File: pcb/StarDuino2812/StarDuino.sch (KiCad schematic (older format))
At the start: 86 parts, among them J1 Screw_Terminal_01x02, J2 Conn_01x03_Male, J3 Conn_01x01_Male, Q1 IRLML6401, U1 ATmega328P-AU, Y1 16M

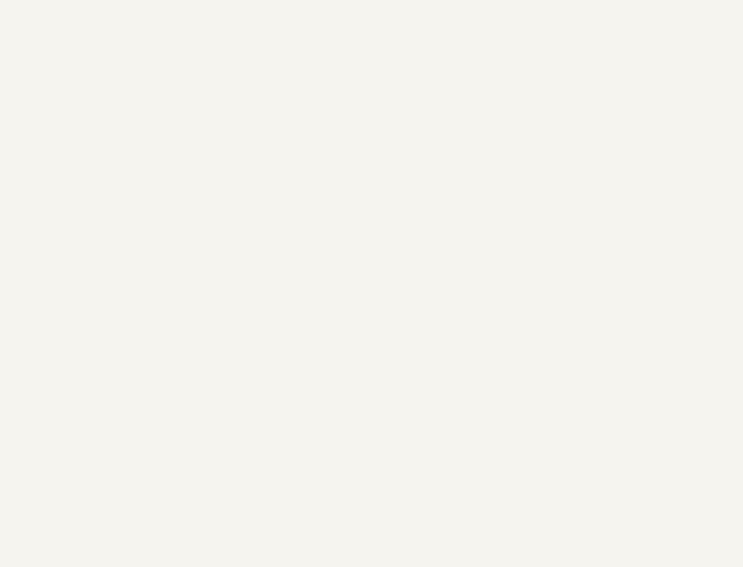
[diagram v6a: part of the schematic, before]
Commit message: NewYearStar2812. Add capacitors.
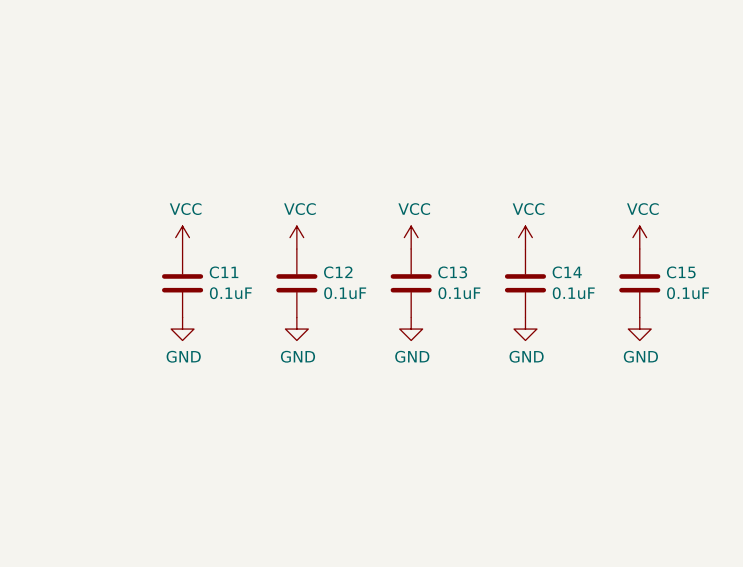
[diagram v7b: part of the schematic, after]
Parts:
- added C11, C12, C13, C14, C15: 0.1uF, Capacitor_THT:C_Rect_L19.0mm_W5.0mm_P15.00mm_MKS4, symbol Device:C
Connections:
- net GND: now also C11.2, C12.2, C13.2, C14.2, C15.2
- net VCC: now also C11.1, C12.1, C13.1, C14.1, C15.1
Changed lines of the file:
@@
 Wire Wire Line
 	4050 6050 4150 6050
+$Comp
+L Device:C C11
+U 1 1 61480CBF
+P 11500 13900
+F 0 "C11" H 11615 13946 50  0000 L CNN
+F 1 "0.1uF" H 11615 13855 50  0000 L CNN
+F 2 "Capacitor_THT:C_Rect_L19.0mm_W5.0mm_P15.00mm_MKS4" H 11538 13750 50  0001 C CNN
+F 3 "~" H 11500 13900 50  0001 C CNN
+	1    11500 13900
+	1    0    0    -1
+$EndComp
+$Comp
+L power:VCC #PWR0145
+U 1 1 61482762
+P 11500 13750
+F 0 "#PWR0145" H 11500 13600 50  0001 C CNN
+F 1 "VCC" H 11515 13923 50  0000 C CNN
+F 2 "" H 11500 13750 50  0001 C CNN
+F 3 "" H 11500 13750 50  0001 C CNN
+	1    11500 13750
+	1    0    0    -1
+$EndComp
+$Comp
+L power:GND #PWR0150
+U 1 1 6148455A
+P 11500 14050
+F 0 "#PWR0150" H 11500 13800 50  0001 C CNN
+F 1 "GND" H 11505 13877 50  0000 C CNN
+F 2 "" H 11500 14050 50  0001 C CNN
+F 3 "" H 11500 14050 50  0001 C CNN
+	1    11500 14050
+	1    0    0    -1
+$EndComp
+$Comp
+L Device:C C12
+U 1 1 6148642E
+P 12000 13900
+F 0 "C12" H 12115 13946 50  0000 L CNN
+F 1 "0.1uF" H 12115 13855 50  0000 L CNN
+F 2 "Capacitor_THT:C_Rect_L19.0mm_W5.0mm_P15.00mm_MKS4" H 12038 13750 50  0001 C CNN
+F 3 "~" H 12000 13900 50  0001 C CNN
+	1    12000 13900
+	1    0    0    -1
+$EndComp
+$Comp
+L power:VCC #PWR0146
+U 1 1 61486434
+P 12000 13750
+F 0 "#PWR0146" H 12000 13600 50  0001 C CNN
+F 1 "VCC" H 12015 13923 50  0000 C CNN
+F 2 "" H 12000 13750 50  0001 C CNN
+F 3 "" H 12000 13750 50  0001 C CNN
+	1    12000 13750
+	1    0    0    -1
+$EndComp
+$Comp
+L power:GND #PWR0151
+U 1 1 6148643A
+P 12000 14050
+F 0 "#PWR0151" H 12000 13800 50  0001 C CNN
+F 1 "GND" H 12005 13877 50  0000 C CNN
+F 2 "" H 12000 14050 50  0001 C CNN
+F 3 "" H 12000 14050 50  0001 C CNN
+	1    12000 14050
+	1    0    0    -1
+$EndComp
+$Comp
+L Device:C C13
+U 1 1 61494103
+P 12500 13900
+F 0 "C13" H 12615 13946 50  0000 L CNN
+F 1 "0.1uF" H 12615 13855 50  0000 L CNN
+F 2 "Capacitor_THT:C_Rect_L19.0mm_W5.0mm_P15.00mm_MKS4" H 12538 13750 50  0001 C CNN
+F 3 "~" H 12500 13900 50  0001 C CNN
+	1    12500 13900
+	1    0    0    -1
+$EndComp
+$Comp
+L power:VCC #PWR0147
+U 1 1 61494109
+P 12500 13750
+F 0 "#PWR0147" H 12500 13600 50  0001 C CNN
+F 1 "VCC" H 12515 13923 50  0000 C CNN
+F 2 "" H 12500 13750 50  0001 C CNN
+F 3 "" H 12500 13750 50  0001 C CNN
+	1    12500 13750
+	1    0    0    -1
+$EndComp
+$Comp
+L power:GND #PWR0152
+U 1 1 6149410F
+P 12500 14050
+F 0 "#PWR0152" H 12500 13800 50  0001 C CNN
+F 1 "GND" H 12505 13877 50  0000 C CNN
+F 2 "" H 12500 14050 50  0001 C CNN
+F 3 "" H 12500 14050 50  0001 C CNN
+	1    12500 14050
+	1    0    0    -1
+$EndComp
+$Comp
+L Device:C C14
+U 1 1 614A1C2E
+P 13000 13900
+F 0 "C14" H 13115 13946 50  0000 L CNN
+F 1 "0.1uF" H 13115 13855 50  0000 L CNN
+F 2 "Capacitor_THT:C_Rect_L19.0mm_W5.0mm_P15.00mm_MKS4" H 13038 13750 50  0001 C CNN
+F 3 "~" H 13000 13900 50  0001 C CNN
+	1    13000 13900
+	1    0    0    -1
+$EndComp
+$Comp
+L power:VCC #PWR0148
+U 1 1 614A1C34
+P 13000 13750
+F 0 "#PWR0148" H 13000 13600 50  0001 C CNN
+F 1 "VCC" H 13015 13923 50  0000 C CNN
+F 2 "" H 13000 13750 50  0001 C CNN
+F 3 "" H 13000 13750 50  0001 C CNN
+	1    13000 13750
+	1    0    0    -1
+$EndComp
+$Comp
+L power:GND #PWR0153
+U 1 1 614A1C3A
+P 13000 14050
+F 0 "#PWR0153" H 13000 13800 50  0001 C CNN
+F 1 "GND" H 13005 13877 50  0000 C CNN
+F 2 "" H 13000 14050 50  0001 C CNN
+F 3 "" H 13000 14050 50  0001 C CNN
+	1    13000 14050
+	1    0    0    -1
+$EndComp
+$Comp
+L Device:C C15
+U 1 1 614AF5BE
+P 13500 13900
+F 0 "C15" H 13615 13946 50  0000 L CNN
+F 1 "0.1uF" H 13615 13855 50  0000 L CNN
+F 2 "Capacitor_THT:C_Rect_L19.0mm_W5.0mm_P15.00mm_MKS4" H 13538 13750 50  0001 C CNN
+F 3 "~" H 13500 13900 50  0001 C CNN
+	1    13500 13900
+	1    0    0    -1
+$EndComp
+$Comp
+L power:VCC #PWR0149
+U 1 1 614AF5C4
+P 13500 13750
+F 0 "#PWR0149" H 13500 13600 50  0001 C CNN
+F 1 "VCC" H 13515 13923 50  0000 C CNN
+F 2 "" H 13500 13750 50  0001 C CNN
+F 3 "" H 13500 13750 50  0001 C CNN
+	1    13500 13750
+	1    0    0    -1
+$EndComp
+$Comp
+L power:GND #PWR0154
+U 1 1 614AF5CA
+P 13500 14050
+F 0 "#PWR0154" H 13500 13800 50  0001 C CNN
+F 1 "GND" H 13505 13877 50  0000 C CNN
+F 2 "" H 13500 14050 50  0001 C CNN
+F 3 "" H 13500 14050 50  0001 C CNN
+	1    13500 14050
+	1    0    0    -1
+$EndComp
 $EndSCHEMATC

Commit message: Replace disk capacitor. Add gerber.
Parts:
- C11, C12, C13, C14, C15: footprint Capacitor_THT:C_Rect_L19.0mm_W5.0mm_P15.00mm_MKS4 -> CommonLibrary:C-disk-15mm
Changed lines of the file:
@@
 F 0 "C11" H 11615 13946 50  0000 L CNN
 F 1 "0.1uF" H 11615 13855 50  0000 L CNN
-F 2 "Capacitor_THT:C_Rect_L19.0mm_W5.0mm_P15.00mm_MKS4" H 11538 13750 50  0001 C CNN
+F 2 "CommonLibrary:C-disk-15mm" H 11538 13750 50  0001 C CNN
 F 3 "~" H 11500 13900 50  0001 C CNN
 	1    11500 13900
@@
 F 0 "C12" H 12115 13946 50  0000 L CNN
 F 1 "0.1uF" H 12115 13855 50  0000 L CNN
-F 2 "Capacitor_THT:C_Rect_L19.0mm_W5.0mm_P15.00mm_MKS4" H 12038 13750 50  0001 C CNN
+F 2 "CommonLibrary:C-disk-15mm" H 12038 13750 50  0001 C CNN
 F 3 "~" H 12000 13900 50  0001 C CNN
 	1    12000 13900
@@
 F 0 "C13" H 12615 13946 50  0000 L CNN
 F 1 "0.1uF" H 12615 13855 50  0000 L CNN
-F 2 "Capacitor_THT:C_Rect_L19.0mm_W5.0mm_P15.00mm_MKS4" H 12538 13750 50  0001 C CNN
+F 2 "CommonLibrary:C-disk-15mm" H 12538 13750 50  0001 C CNN
 F 3 "~" H 12500 13900 50  0001 C CNN
 	1    12500 13900
@@
 F 0 "C14" H 13115 13946 50  0000 L CNN
 F 1 "0.1uF" H 13115 13855 50  0000 L CNN
-F 2 "Capacitor_THT:C_Rect_L19.0mm_W5.0mm_P15.00mm_MKS4" H 13038 13750 50  0001 C CNN
+F 2 "CommonLibrary:C-disk-15mm" H 13038 13750 50  0001 C CNN
 F 3 "~" H 13000 13900 50  0001 C CNN
 	1    13000 13900
@@
 F 0 "C15" H 13615 13946 50  0000 L CNN
 F 1 "0.1uF" H 13615 13855 50  0000 L CNN
-F 2 "Capacitor_THT:C_Rect_L19.0mm_W5.0mm_P15.00mm_MKS4" H 13538 13750 50  0001 C CNN
+F 2 "CommonLibrary:C-disk-15mm" H 13538 13750 50  0001 C CNN
 F 3 "~" H 13500 13900 50  0001 C CNN
 	1    13500 13900
